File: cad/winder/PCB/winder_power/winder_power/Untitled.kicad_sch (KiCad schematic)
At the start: 17 parts, among them Q1 IRF4905

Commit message: パーツリストMDを作成
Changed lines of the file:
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@@
-	)
-	(junction
-		(at 139.7 102.87)
-		(diameter 0)
-		(color 0 0 0 0)
 	)
 	(junction
@@
 	)
 	(junction
+		(at 138.43 102.87)
+		(diameter 0)
+		(color 0 0 0 0)
+	)
+	(junction
 		(at 106.68 57.15)
 		(diameter 0)
@@
 	(wire
 		(pts
-			(xy 139.7 102.87) (xy 130.81 102.87)
+			(xy 138.43 96.52) (xy 139.7 96.52)
+		)
+		(stroke
+			(width 0)
+			(type default)
+		)
+	)
+	(wire
+		(pts
+			(xy 138.43 102.87) (xy 157.48 102.87)
 		)
 		(stroke
@@
 	(wire
 		(pts
-			(xy 139.7 96.52) (xy 139.7 102.87)
+			(xy 138.43 96.52) (xy 138.43 102.87)
 		)
 		(stroke
@@
 	(wire
 		(pts
+			(xy 138.43 102.87) (xy 130.81 102.87)
+		)
+		(stroke
+			(width 0)
+			(type default)
+		)
+	)
+	(wire
+		(pts
 			(xy 138.43 60.96) (xy 138.43 68.58)
 		)
@@
 		)
 		(stroke
-			(width 0)
-			(type default)
-		)
-	)
-	(wire
-		(pts
-			(xy 157.48 102.87) (xy 139.7 102.87)
-		)
-		(stroke

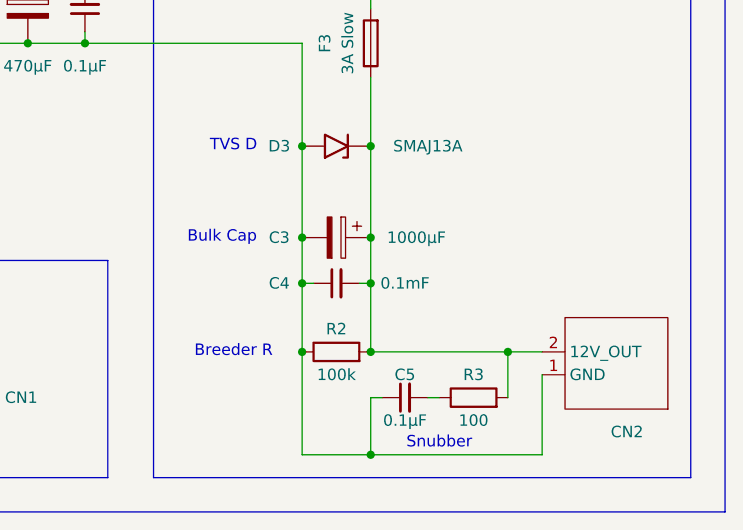
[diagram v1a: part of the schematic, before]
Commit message: Fix winder asset naming and BOM units
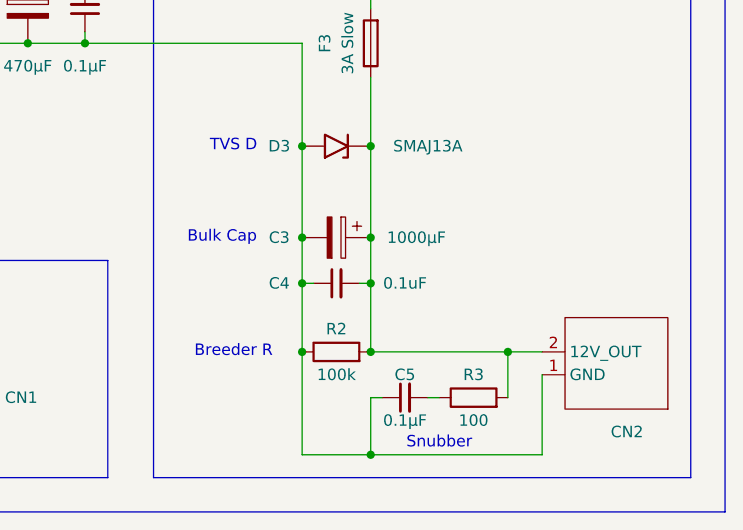
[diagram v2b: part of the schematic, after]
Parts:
- C4: value 0.1mF -> 0.1uF
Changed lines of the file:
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@@
 			)
 		)
-		(property "Value" "0.1mF"
+		(property "Value" "0.1uF"
 			(at 142.24 83.82 90)
 			(effects
